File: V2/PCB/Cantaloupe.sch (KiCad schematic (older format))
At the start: 124 parts, among them J1 USB_In, J2 OLED, J3 Link, J4 Debug, J5 Trackball, Q1 2N7002, Q2 AO3401A, SW1 MX, SW10 MX, SW11 MX, SW12 MX, SW13 MX, SW14 MX, SW15 MX, SW16 MX, SW17 MX, SW18 MX, SW19 MX, SW2 MX, SW20 MX, SW21 MX, SW22 MX, SW23 MX, SW24 MX, SW25 MX, SW26 MX, SW27 MX, SW28 MX, SW29 MX, SW3 MX, SW30 MX, SW31 Encoder, SW32 MX, SW4 MX, SW5 MX, SW6 MX, SW7 MX, SW8 MX, SW9 MX, U1 STM32F4x1CxUx, U2 SRV05-4, U3 SRV05-4, U4 XC6206P332MR, U5 LMV321, Y1 8MHz

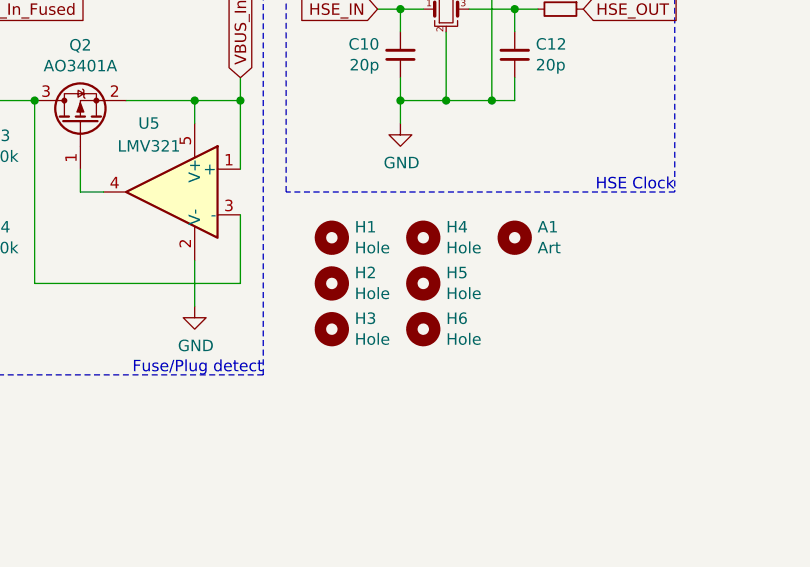
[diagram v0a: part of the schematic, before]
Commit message: New plate files, removed internal holes from PCB
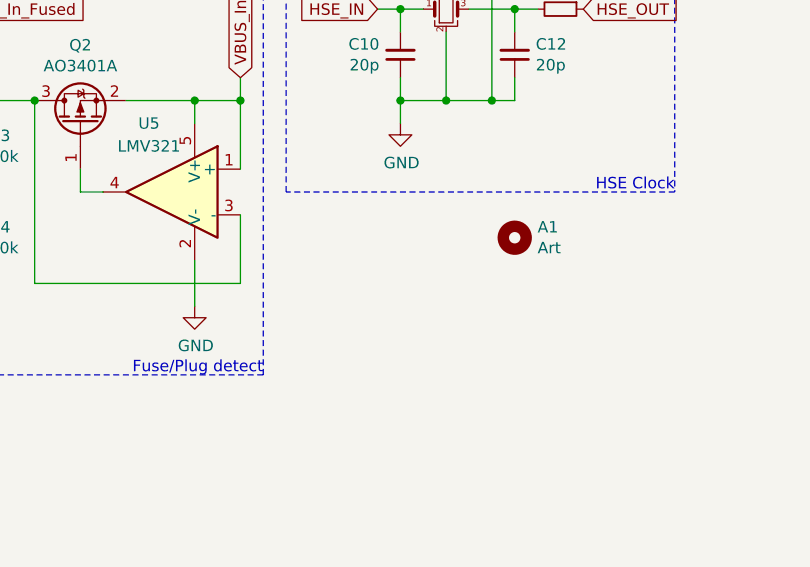
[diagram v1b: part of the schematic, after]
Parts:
- removed H1, H2, H3, H4, H5, H6: Hole, Ariamelon:HOLE_M2_TH, symbol Mechanical:MountingHole
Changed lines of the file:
@@
 VBUS_In
-$Comp
-L Mechanical:MountingHole H1
-U 1 1 62077E70
-P 8700 5500
-F 0 "H1" H 8800 5546 50  0000 L CNN
-F 1 "Hole" H 8800 5455 50  0000 L CNN
-F 2 "Ariamelon:HOLE_M2_TH" H 8700 5500 50  0001 C CNN
-F 3 "~" H 8700 5500 50  0001 C CNN
-	1    8700 5500
-	1    0    0    -1
-$EndComp
-$Comp
-L Mechanical:MountingHole H2
-U 1 1 62096D2A
-P 8700 5700
-F 0 "H2" H 8800 5746 50  0000 L CNN
-F 1 "Hole" H 8800 5655 50  0000 L CNN
-F 2 "Ariamelon:HOLE_M2_TH" H 8700 5700 50  0001 C CNN
-F 3 "~" H 8700 5700 50  0001 C CNN
-	1    8700 5700
-	1    0    0    -1
-$EndComp
-$Comp
-L Mechanical:MountingHole H3
-U 1 1 6209708C
-P 8700 5900
-F 0 "H3" H 8800 5946 50  0000 L CNN
-F 1 "Hole" H 8800 5855 50  0000 L CNN
-F 2 "Ariamelon:HOLE_M2_TH" H 8700 5900 50  0001 C CNN
-F 3 "~" H 8700 5900 50  0001 C CNN
-	1    8700 5900
-	1    0    0    -1
-$EndComp
-$Comp
-L Mechanical:MountingHole H4
-U 1 1 62097F05
-P 9100 5500
-F 0 "H4" H 9200 5546 50  0000 L CNN
-F 1 "Hole" H 9200 5455 50  0000 L CNN
-F 2 "Ariamelon:HOLE_M2_TH" H 9100 5500 50  0001 C CNN
-F 3 "~" H 9100 5500 50  0001 C CNN
-	1    9100 5500
-	1    0    0    -1
-$EndComp
-$Comp
-L Mechanical:MountingHole H5
-U 1 1 62097F0B
-P 9100 5700
-F 0 "H5" H 9200 5746 50  0000 L CNN
-F 1 "Hole" H 9200 5655 50  0000 L CNN
-F 2 "Ariamelon:HOLE_M2_TH" H 9100 5700 50  0001 C CNN
-F 3 "~" H 9100 5700 50  0001 C CNN
-	1    9100 5700
-	1    0    0    -1
-$EndComp
-$Comp
-L Mechanical:MountingHole H6
-U 1 1 62097F11
-P 9100 5900
-F 0 "H6" H 9200 5946 50  0000 L CNN
-F 1 "Hole" H 9200 5855 50  0000 L CNN
-F 2 "Ariamelon:HOLE_M2_TH" H 9100 5900 50  0001 C CNN
-F 3 "~" H 9100 5900 50  0001 C CNN
-	1    9100 5900
-	1    0    0    -1
-$EndComp
 $Comp
 L Mechanical:MountingHole A1

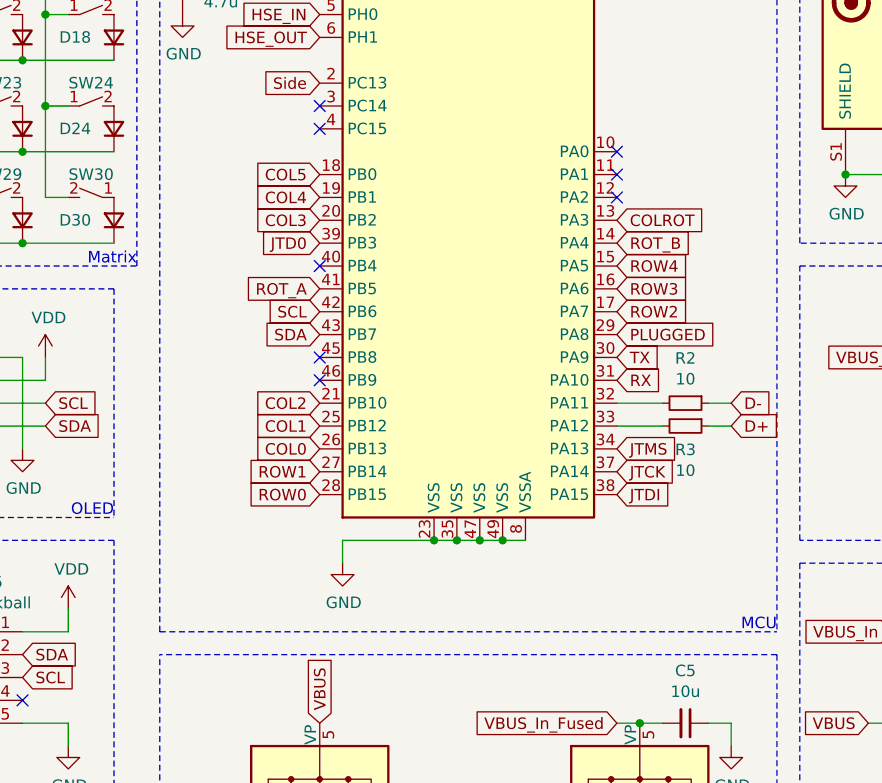
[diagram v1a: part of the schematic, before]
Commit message: Fixed issues with PCB
Changed pin assignments so B2 isn't used. Added pull-up for RX pin and pull-down for B2 pin so it can properly load into the bootloader.
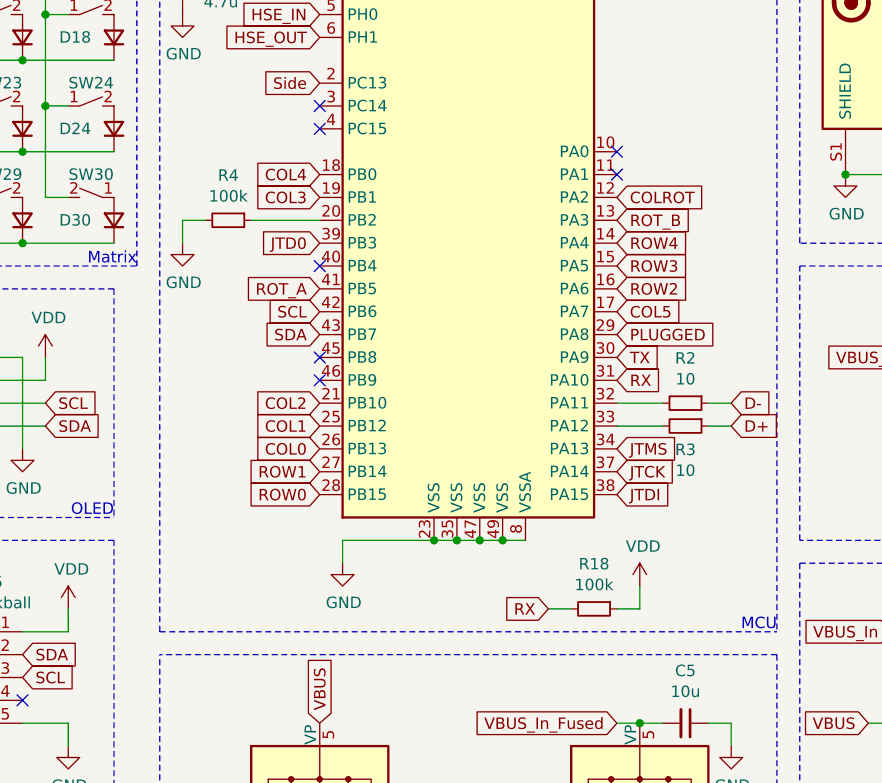
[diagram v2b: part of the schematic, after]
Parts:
- added R18, R4: 100k, Resistor_SMD:R_0603_1608Metric, symbol Device:R_Small
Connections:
- net COL3: now also U1.19 (PB1); no longer U1.20 (PB2)
- net COL4: now also U1.18 (PB0); no longer U1.19 (PB1)
- net COL5: now also U1.17 (PA7); no longer U1.18 (PB0)
- net COLROT: now also U1.12 (PA2); no longer U1.13 (PA3)
- net GND: now also R4.2
- net ROT_B: now also U1.13 (PA3); no longer U1.14 (PA4)
- net ROW2: now also U1.16 (PA6); no longer U1.17 (PA7)
- net ROW3: now also U1.15 (PA5); no longer U1.16 (PA6)
- net ROW4: now also U1.14 (PA4); no longer U1.15 (PA5)
- net RX: now also R18.2
- net VDD: now also R18.1
- new net: R4.1, U1.20 (PB2)
- no-connect marks 19 -> 18
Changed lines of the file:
@@
 Text GLabel 4300 3800 0    50   Input ~ 0
 ROW1
-Text GLabel 4300 2700 0    50   Input ~ 0
+Text GLabel 4300 2600 0    50   Input ~ 0
 COL3
-Text GLabel 4300 2600 0    50   Input ~ 0
+Text GLabel 4300 2500 0    50   Input ~ 0
 COL4
-Text GLabel 4300 2500 0    50   Input ~ 0
+Text GLabel 5600 3100 2    50   Input ~ 0
 COL5
-Text GLabel 5600 3100 2    50   Input ~ 0
+Text GLabel 5600 3000 2    50   Input ~ 0
 ROW2
-Text GLabel 5600 3000 2    50   Input ~ 0
+Text GLabel 5600 2900 2    50   Input ~ 0
 ROW3
-Text GLabel 5600 2900 2    50   Input ~ 0
+Text GLabel 5600 2800 2    50   Input ~ 0
 ROW4
+Text GLabel 5600 2600 2    50   Input ~ 0
+COLROT
 Text GLabel 5600 2700 2    50   Input ~ 0
-COLROT
-Text GLabel 5600 2800 2    50   Input ~ 0
 ROT_B
 Wire Wire Line
@@
 NoConn ~ 5600 2400
 NoConn ~ 5600 2500
-NoConn ~ 5600 2600
 Text GLabel 9600 1200 0    50   Input ~ 0
 TX
@@
 Wire Notes Line
 	10600 600  10600 2800
+$Comp
+L Device:R_Small R4
+U 1 1 620B74EB
+P 3900 2700
+F 0 "R4" V 3704 2700 50  0000 C CNN
+F 1 "100k" V 3795 2700 50  0000 C CNN
+F 2 "Resistor_SMD:R_0603_1608Metric" H 3900 2700 50  0001 C CNN
+F 3 "~" H 3900 2700 50  0001 C CNN
+	1    3900 2700
+	0    1    1    0
+$EndComp
+Wire Wire Line
+	4000 2700 4300 2700
+$Comp
+L power:GND #PWR0133
+U 1 1 620CAA5D
+P 3700 2800
+F 0 "#PWR0133" H 3700 2550 50  0001 C CNN
+F 1 "GND" H 3705 2627 50  0000 C CNN
+F 2 "" H 3700 2800 50  0001 C CNN
+F 3 "" H 3700 2800 50  0001 C CNN
+	1    3700 2800
+	1    0    0    -1
+$EndComp
+Wire Wire Line
+	3700 2800 3700 2700
+Wire Wire Line
+	3700 2700 3800 2700
+Text GLabel 5300 4400 0    50   Input ~ 0
+RX
+$Comp
+L Device:R_Small R18
+U 1 1 620DECC4
+P 5500 4400
+F 0 "R18" V 5304 4400 50  0000 C CNN
+F 1 "100k" V 5395 4400 50  0000 C CNN
+F 2 "Resistor_SMD:R_0603_1608Metric" H 5500 4400 50  0001 C CNN
+F 3 "~" H 5500 4400 50  0001 C CNN
+	1    5500 4400
+	0    1    1    0
+$EndComp
+$Comp
+L power:VDD #PWR0134
+U 1 1 620F089D
+P 5700 4300
+F 0 "#PWR0134" H 5700 4150 50  0001 C CNN
+F 1 "VDD" H 5715 4473 50  0000 C CNN
+F 2 "" H 5700 4300 50  0001 C CNN
+F 3 "" H 5700 4300 50  0001 C CNN
+	1    5700 4300
+	1    0    0    -1
+$EndComp
+Wire Wire Line
+	5700 4300 5700 4400
+Wire Wire Line
+	5700 4400 5600 4400
+Wire Wire Line
+	5300 4400 5400 4400
 $EndSCHEMATC

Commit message: Fixed many issues with the board
Changed pin assignments so B2 isn't used. Added pull-up for RX pin and pull-down for B2 pin so the keyboard can properly load into the bootloader. Changed reset circuit so it actually works. Removed USB series resistors. Removed non-functional JTAG pins. Changed SRV05-04 to SRV0504. Thanks to sigprof and MasterSpoon from the QMK discord server for the help!
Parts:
- added D33: D, Ariamelon:D_SOD-123, symbol Device:D_Small
- C4: value 1u -> 100n
- J4: symbol Connector_Generic:Conn_01x06 -> Connector_Generic:Conn_01x04
- R11: value 10k -> 1M
- R2: value 10 -> 330k
- R3: value 10 -> 1k
- R9: value 100k -> 100
- U2, U3: value SRV05-4 -> SRV0504
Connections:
- net BOOT0: now also C2.1, R11.1, R2.1; no longer C2.2, R7.2, SW32.1 (A)
- net D+: now also U1.33 (PA12); no longer R3.1
- net D-: now also U1.32 (PA11); no longer R2.1
- net GND: now also C2.2, J4.4 (Pin_4), R11.2; no longer J4.6 (Pin_6), R9.2
- net NRST: now also R9.2; no longer Q1.3 (D), R11.2
- net VBUS: no longer U2.5 (VP)
- net VBUS_In: now also U2.5 (VP)
- net VDD: no longer R11.1
- net at R2.2: now also D33.1 (K); no longer U1.32 (PA11)
- net at R3.2: now also Q1.1 (G), R7.2; no longer U1.33 (PA12)
- net JTCK renamed SWOCLK
- net JTD0: no longer names the net of U1.39 (PB3)
- net JTD0: no longer J4.4 (Pin_4)
- net JTDI: no longer names the net of U1.38 (PA15)
- net JTDI: no longer J4.5 (Pin_5)
- net JTMS renamed SWOIO
- new net: D33.2 (A), R3.1, SW32.1 (A)
- new net: Q1.3 (D), R9.1
- no-connect marks 18 -> 20
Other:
- moved on the sheet: A1, C10, C12, C2, C4, JP1, JP2, Q1, R16, R17, R7, R9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
